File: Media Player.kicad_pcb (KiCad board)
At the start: 4 copper layers, 114.3 x 68.5 mm, 144 parts, among them J1 12402012E212A, J10 MEM2075-00-140-01-A, J40 PH2.0, J41 UART, J70 SJ-3524-SMT-TR, Q10 DMP3068L-7, Q40 DMP3068L-7, Q50 DMP3068L-7, Q70 DMP3068L-7, SW30 BOOT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

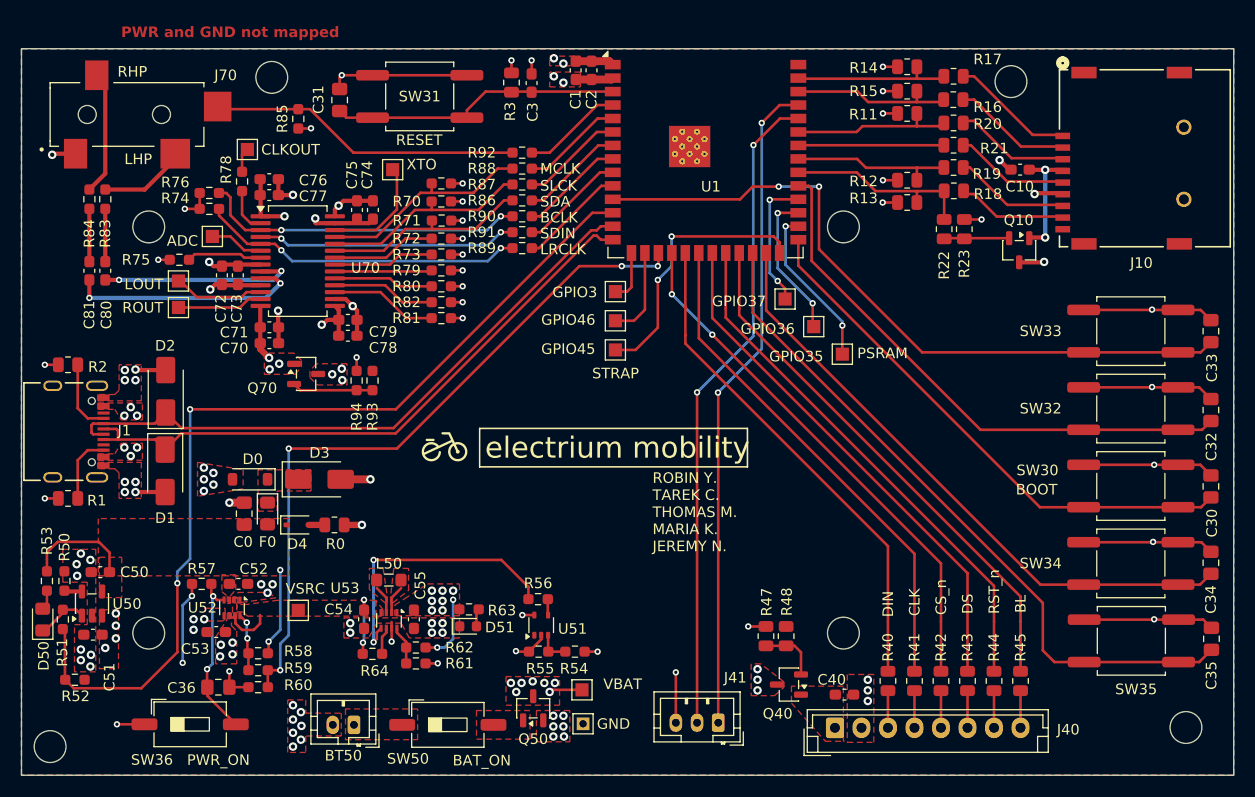
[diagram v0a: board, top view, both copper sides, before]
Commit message: Ground Stitching, PMOS 0-Res Moved,
DRC should be near cleared. Might want to reconsider mapping some pin functions? SD card detect line, also battery checker (making use of comparator). Also, double check if audio IC microphone pins (and ADC) are supposed to be pulled to VMID
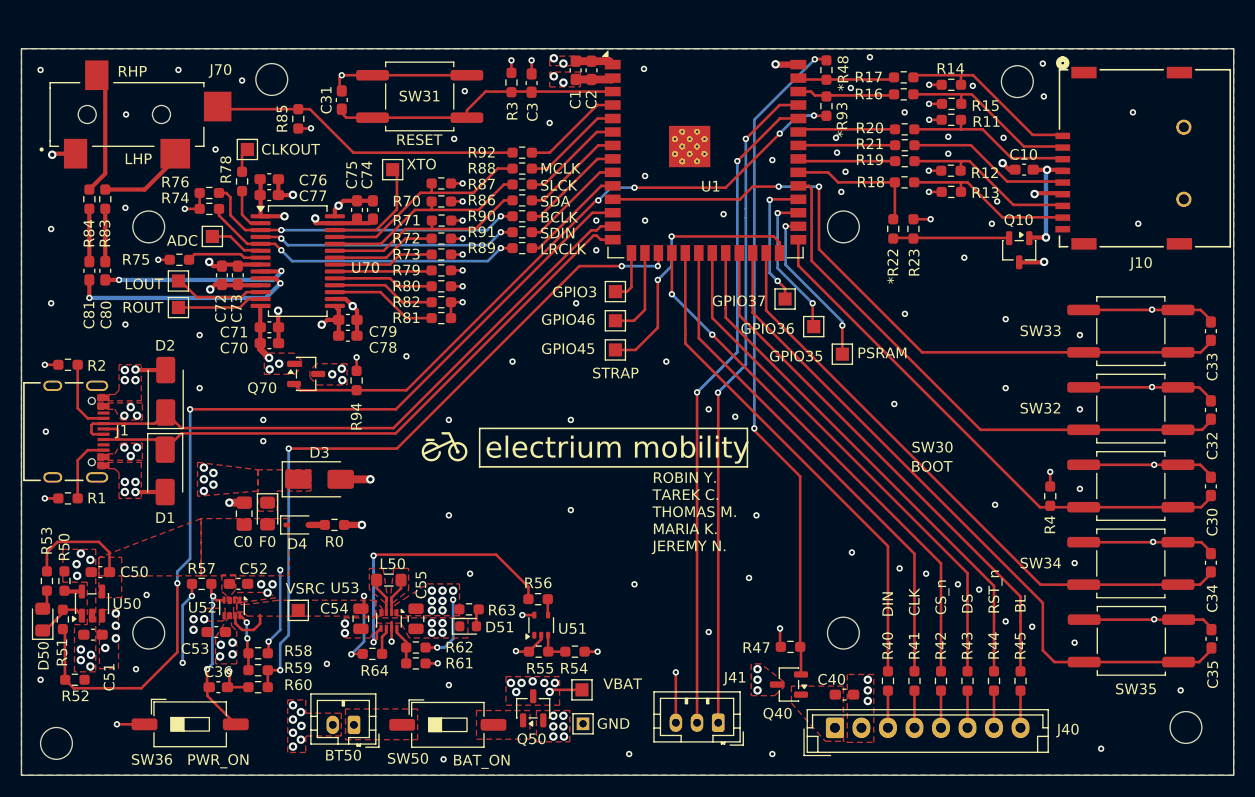
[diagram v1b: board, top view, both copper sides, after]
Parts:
- removed D0: 1N5819HW-7-F, Diode_SMD:D_SOD-123
- added R4: 10kΩ, Resistor_SMD:R_0603_1608Metric_Pad0.98x0.95mm_HandSolder, F.Cu at (183.2, 82.2)
- *R22: renamed from R22; footprint Resistor_SMD:R_0805_2012Metric -> Resistor_SMD:R_0603_1608Metric_Pad0.98x0.95mm_HandSolder
- *R48: renamed from R48; footprint Resistor_SMD:R_0805_2012Metric -> Resistor_SMD:R_0603_1608Metric_Pad0.98x0.95mm_HandSolder
- C30: value 0.1uF -> 1uF; footprint Capacitor_SMD:C_0805_2012Metric_Pad1.18x1.45mm_HandSolder -> Capacitor_SMD:C_0603_1608Metric_Pad1.08x0.95mm_HandSolder
- C31, C32, C33, C34, C35, C36: footprint Capacitor_SMD:C_0805_2012Metric_Pad1.18x1.45mm_HandSolder -> Capacitor_SMD:C_0603_1608Metric_Pad1.08x0.95mm_HandSolder
- C54, C55: footprint Capacitor_SMD:C_0603_1608Metric_Pad1.08x0.95mm_HandSolder -> Capacitor_SMD:C_0805_2012Metric
- R0, R1, R11, R12, R13, R14, R15, R16, R17, R18, R19, R2, R20, R21, R23, R3, R40, R41, R42, R43, R44, R45, R47: footprint Resistor_SMD:R_0805_2012Metric -> Resistor_SMD:R_0603_1608Metric_Pad0.98x0.95mm_HandSolder
- moved *R48 53.5 mm to (162.1, 42.0), turned to -90 degrees
- moved *R93 50.0 mm to (162.1, 45.4)
- moved *R22 4.80 mm to (168.4, 57.0)
- moved R23 4.80 mm to (170.3, 57.0)
- moved R18 4.72 mm to (169.5, 52.6)
- moved R16 4.70 mm to (169.4, 44.3)
- moved R17 4.70 mm to (169.4, 42.7)
- moved R20 4.65 mm to (169.5, 47.6)
- moved R19 4.64 mm to (169.5, 50.6)
- moved R21 4.60 mm to (169.5, 49.1)
- moved R14 4.50 mm to (173.9, 43.4)
- moved R15 4.36 mm to (173.9, 45.2)
- moved R13 4.28 mm to (173.9, 53.5)
- moved R12 4.22 mm to (173.8, 51.5)
- moved R11 4.21 mm to (173.9, 46.7)
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- renumbered R93 to *R93
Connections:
- D3 pad 1: /USB_PWR2 -> /USB_PWR
- F0 pad 1: /USB_PWR2 -> /USB_PWR
- J10 pad P1: Net-(J10-DAT2) -> /D2
- J10 pad P2: Net-(J10-CD/DAT3) -> /D3
- J10 pad P3: Net-(J10-CMD) -> /CMD
- J10 pad P7: Net-(J10-DAT0) -> /D0
- J10 pad P8: Net-(J10-DAT1) -> /D1
- R11 pad 1: /SD_CMD -> /CMD
- R12 pad 1: /SD_D0 -> /D0
- R13 pad 1: /SD_D1 -> /D1
- R14 pad 1: /SD_D2 -> /D2
- R15 pad 1: /SD_D3 -> /D3
- R16 pad 1: Net-(J10-CD/DAT3) -> /D3
- R17 pad 1: Net-(J10-DAT2) -> /D2
- R18 pad 1: Net-(J10-DAT1) -> /D1
- R19 pad 1: Net-(J10-DAT0) -> /D0
- R20 pad 2: Net-(J10-CMD) -> /CMD
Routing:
- net Net-(Q40-G): track 5.65 -> 62.8 mm, vias 0 -> 2
- net /AudioAlt/PWR_CTRL: track 7.64 -> 61.1 mm, vias 0 -> 4
- net /D2: track 0.00 -> 17.7 mm
- net /D3: track 0.00 -> 17.5 mm
- net /D0: track 0.00 -> 17.1 mm
- net /D1: track 0.00 -> 16.5 mm
- net /CMD: track 0.00 -> 16.3 mm
- net Net-(J10-DAT2): track 12.0 -> 0.00 mm
- net Net-(J10-CD/DAT3): track 11.6 -> 0.00 mm
- net Net-(J10-CMD): track 11.2 -> 0.00 mm
- net Net-(J10-DAT0): track 11.2 -> 0.00 mm
- net Net-(J10-DAT1): track 10.6 -> 0.00 mm
- net /SD_CMD: track 15.4 -> 9.27 mm
- net /SD_D0: track 15.3 -> 9.21 mm
- net /SD_D2: track 14.9 -> 9.16 mm
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- removed copper zone on F.Cu, net /USB_PWR2
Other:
- outline, holes or cut-outs redrawn
- board text added: "Find a way to implement card detect pin 9 Confirm Audio connections --> mainly i2c and microphone VMID stuff Maybe for future update, you might want someway to detect battery voltage analog, and instead of a comparator as either 0/1."
- board text removed: "Change gnd traces on USB and SDIO to copper pour (need stitching?)"
- board text removed: "Changed pad clearance for USB because manufacturer footprint is designed wrong."
- board text removed: "Check out copper pour priority override"
- board text removed: "Check with Damir the thickness of dielectric and copper"
- board text removed: "PWR and GND not mapped"
- board text removed: "Use calculator for trace widths for power Might need to change design constraints for better power routing"
- board text removed: "move pwr_src down and connect vsrc from outside the IC too, use via to connect to pwr_src"
- board text removed: "widen vsrc trace or shorten"

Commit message: UNFINISHED: Rerouted Traces, new LEDs, replaced components
Removed charging status and power source signals from MCU and gave them their own LEDs. Added analog battery voltage and card detect as replacement. Also found out not all components are in stock... troubling to find replacements :( should have done this during schematic
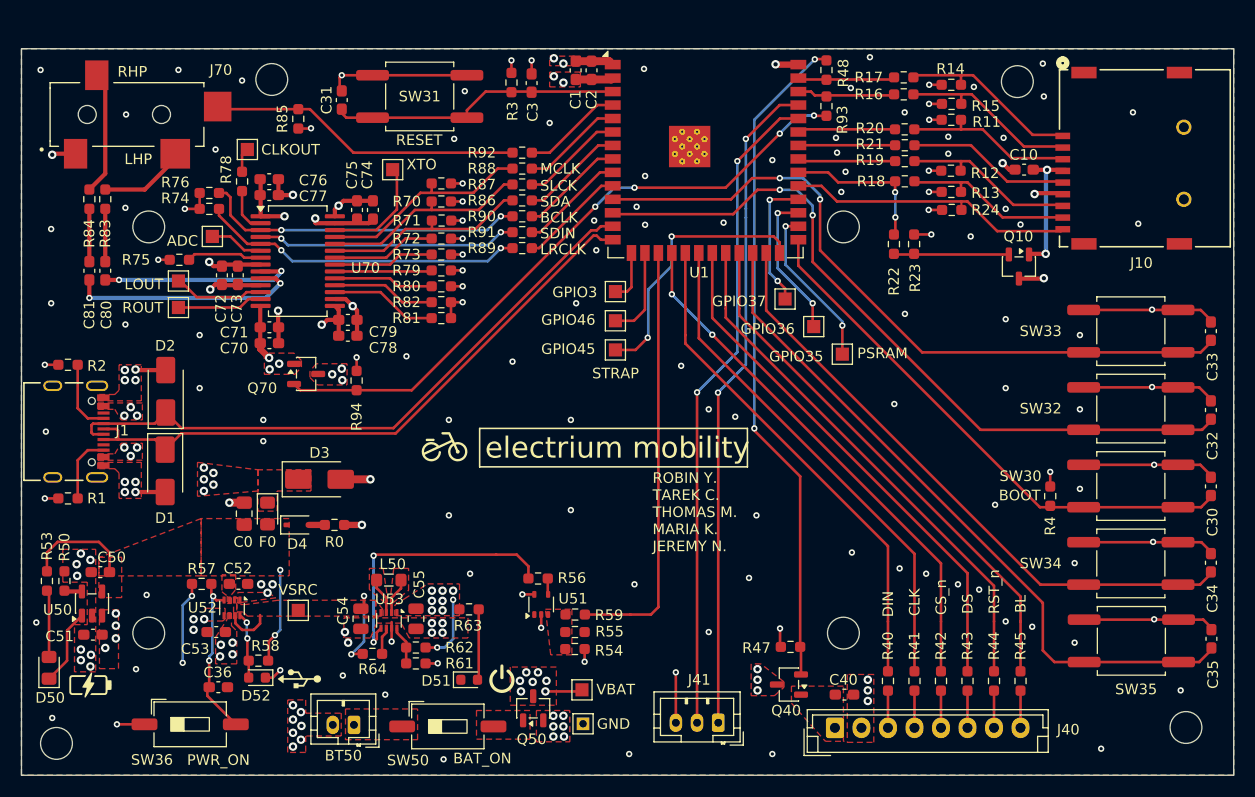
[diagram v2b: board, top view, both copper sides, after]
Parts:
- removed R51: 2.2kΩ, Resistor_SMD:R_0603_1608Metric_Pad0.98x0.95mm_HandSolder
- removed R52: 4.3kΩ, Resistor_SMD:R_0603_1608Metric_Pad0.98x0.95mm_HandSolder
- removed R60: 10kΩ, Resistor_SMD:R_0603_1608Metric_Pad0.98x0.95mm_HandSolder
- added D52: BLUE, LED_SMD:LED_0603_1608Metric, F.Cu at (108.4, 99.3)
- added G***: LOGO, LOGO, F.Cu at (112.4, 99.4)
- added G***: LOGO, LOGO, F.Cu at (92.7, 100.0)
- added G***: LOGO, LOGO, F.Cu at (131.5, 99.4)
- added R24: 10kΩ, Resistor_SMD:R_0603_1608Metric_Pad0.98x0.95mm_HandSolder, F.Cu at (173.9, 55.2)
- R59: value 5.1kΩ -> 0Ω
- moved R59 30.4 mm to (138.4, 93.3)
- moved D51 5.04 mm to (128.4, 99.5)
- moved D50 4.59 mm to (88.8, 98.4)
- moved R55 3.89 mm to (138.4, 95.0), turned to 180 degrees
- moved R56 1.95 mm to (134.9, 90.0)
- moved U51 1.95 mm to (135.2, 92.4)
- moved Q10 1.54 mm to (180.2, 60.5)
- moved R22 1.44 mm to (168.5, 58.4)
- moved R23 1.44 mm to (170.4, 58.4)
- moved R58 0.70 mm to (108.5, 97.7)
- moved R54 0.25 mm to (138.4, 96.6)
- moved SW50 0.15 mm to (126.4, 103.9)
- moved R18 0.10 mm to (169.5, 52.5)
- renumbered *R22 to R22, *R48 to R48, *R93 to R93
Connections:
- net /PWR_SRC renamed /BAT_LEV
- J10 pad P9: (no net) -> /SD_CD
- R58 pad 2: Net-(U52-ST) -> Net-(D52-A)
- R59 pad 1: Net-(U52-ST) -> Net-(U51-+)
- U1 pad 12: /CHRG_STAT -> /PB0
- U1 pad 31: /PB0 -> /SD_CD
- U52 pad 8: Net-(U52-ST) -> Net-(D52-A)
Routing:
- net /CHRG_STAT: track 88.0 -> 0.00 mm, vias 2 -> 0
- net /SD_CD: track 0.00 -> 27.6 mm
- net /BAT_LEV: track 67.3 -> 40.6 mm, vias 4 -> 0
- net /PB0: track 52.8 -> 70.2 mm, vias 0 -> 2
- net Net-(D52-A): track 0.00 -> 6.18 mm, vias 0 -> 2
- net Net-(U52-ST): track 5.47 -> 0.00 mm, vias 2 -> 0
- net Net-(D51-A): track 1.69 -> 6.69 mm
- net Net-(D50-A): track 1.76 -> 6.33 mm
- net GND: track 154.2 -> 150.5 mm, vias 166 -> 168
- net Net-(U51-+): track 3.16 -> 0.00 mm
- net /Power/STAT: track 4.54 -> 7.23 mm
- net /SD_D1: track 13.3 -> 15.0 mm, vias 0 -> 2
- net /SD_VDD: track 11.1 -> 12.7 mm
- net +3V3: track 25.5 -> 26.9 mm, vias 28 -> 29
- net /Power/BB_EN: track 26.8 -> 26.0 mm
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- added copper zone on F.Cu, net Net-(U51-+)

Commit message: New Audio Jack
Replaced audio jack with actually available component from xunpu, changed MIC845 to MIC841. Still need to double check the audio codec
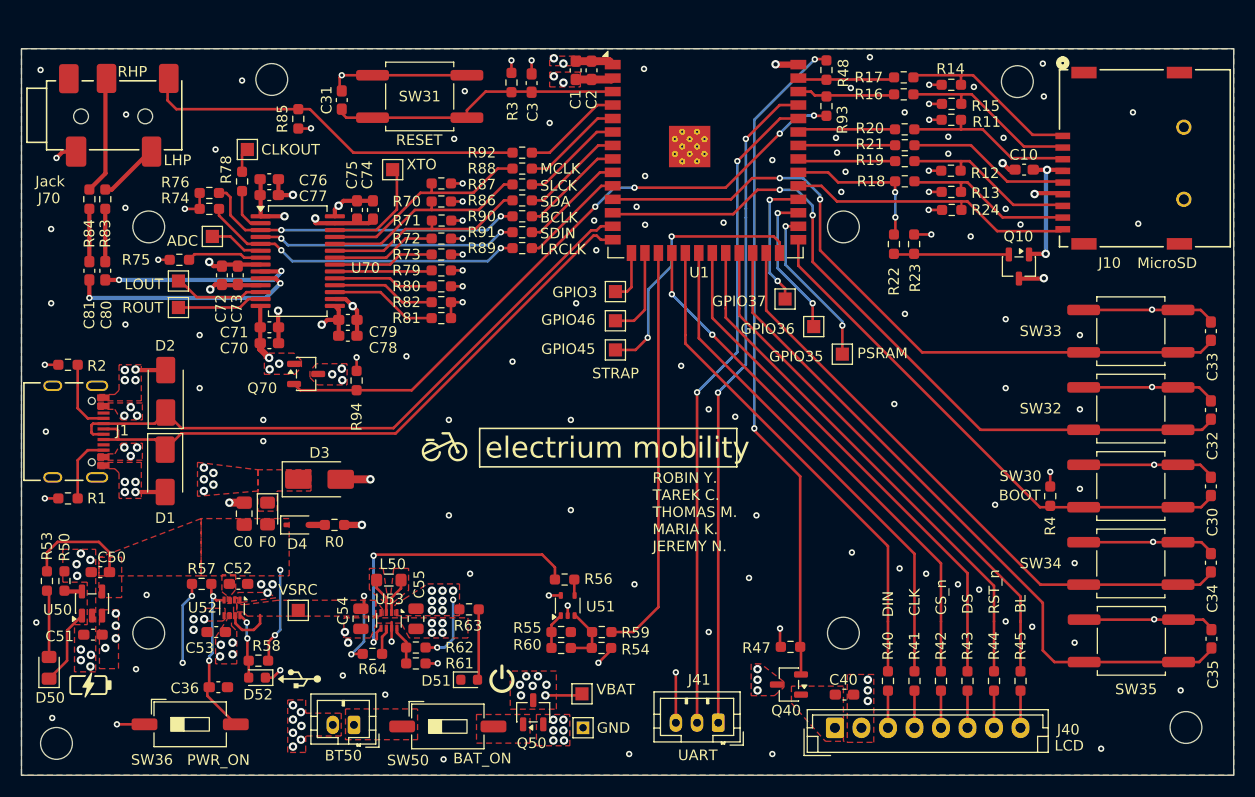
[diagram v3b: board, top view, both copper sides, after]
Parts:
- added R60: 10kΩ, Resistor_SMD:R_0603_1608Metric_Pad0.98x0.95mm_HandSolder, F.Cu at (137.1, 96.5)
- J70: value SJ-3524-SMT-TR -> PJ-327C-4A; footprint Footprints:CUI_SJ-3524-SMT -> Footprints:Korean Hroparts Elec PJ-327C-4A
- R54: value 2.7kΩ -> 200kΩ
- R55: value 10kΩ -> 110kΩ
- U50: value MCP73831-2-OT -> MCP73831-2DCI/MC
- U51: value MIC845H -> MIC841L
- moved J70 5.23 mm to (89.3, 50.4)
- moved R59 3.00 mm to (140.9, 95.0)
- moved R54 2.50 mm to (140.9, 96.5)
- moved R56 2.50 mm to (137.4, 90.0)
- moved U51 2.50 mm to (137.7, 92.5)
- moved R55 1.30 mm to (137.1, 95.0)
- moved Q50 0.38 mm to (134.4, 102.6)
- moved TP50 0.38 mm to (139.1, 100.8)
- moved TP51 0.38 mm to (139.2, 104.0)
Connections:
- R54 pad 1: Net-(U51-+) -> Net-(U51-LTH)
- R55 pad 2: Net-(U51-+) -> Net-(U51-HTH)
- R59 pad 1: Net-(U51-+) -> Net-(U51-LTH)
- U51 pad 1: unconnected-(U51-NIC-Pad1) -> Net-(U51-HTH)
- U51 pad 3: Net-(U51-+) -> Net-(U51-LTH)
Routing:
- net /AudioAlt/A2_TSW: track 30.1 -> 36.6 mm
- net Net-(U51-LTH): track 0.00 -> 5.77 mm
- net Net-(U51-HTH): track 0.00 -> 3.41 mm
- net Net-(J70-PadT): track 8.50 -> 5.68 mm
- net /Power/BB_EN: track 26.0 -> 28.6 mm
- net /BAT_LEV: track 40.6 -> 38.8 mm
- net GND: track 150.5 -> 149.6 mm, vias 168 -> 167
- removed copper zone on F.Cu, net Net-(U51-+)
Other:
- board text added: "Jack"
- board text added: "LCD"
- board text added: "MicroSD"
- board text added: "UART"

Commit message: No changes made.
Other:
- board text added: "Confirm Audio connections --> mainly i2c and microphone VMID stuff Check Silkscreen thickeness Look for floating connections/unnecessary curves on traces Make sure audio jack switch is pulled correctly ASK GPT FOR MORE THINGS TO DOUBLE CHECK pls pls pls double check mounting hole positioning Confirm all IC's are using the right footprints Spend time reading over all datasheets again :sob:"
- board text removed: "Double check that your that your parts are IN STOCK"
- board text removed: "Find a way to implement card detect pin 9 Confirm Audio connections --> mainly i2c and microphone VMID stuff Maybe for future update, you might want someway to detect battery voltage analog, and instead of a comparator as either 0/1."
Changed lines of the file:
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@@
 		)
 	)
-	(gr_text "Double check that your that your parts are IN STOCK"
-		(at 206 63.1 0)
+	(gr_text "Confirm Audio connections --> mainly i2c and microphone VMID stuff\nCheck Silkscreen thickeness\nLook for floating connections/unnecessary curves on traces\nMake sure audio jack switch is pulled correctly\nASK GPT FOR MORE THINGS TO DOUBLE CHECK\npls pls pls double check mounting hole positioning\nConfirm all IC's are using the right footprints\nSpend time reading over all datasheets again :sob:"
+		(at 205 79.8 0)
 		(layer "User.1")
 		(effects
-			(font
-				(size 1 1)
-				(thickness 0.15)
-			)
-			(justify left bottom)
-		)
-	)
-	(gr_text "Find a way to implement card detect pin 9\nConfirm Audio connections --> mainly i2c and microphone VMID stuff\nMaybe for future update, you might want someway to detect battery voltage\nanalog, and instead of a comparator as either 0/1."
-		(at 212.6 81.7 0)
-		(layer "User.1")
-		(effects
